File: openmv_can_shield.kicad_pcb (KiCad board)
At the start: 2 copper layers, 75 x 49 mm, 32 parts, among them J1 WAGO_250-204, J2 Pulse_JXD6-0001NL, J3 Conn_01x03, J4 Conn_01x02, J5 Conn_02x03_Odd_Even, J6 Conn_02x05_Odd_Even, J7 Conn_01x02, J8 Conn_01x02, Q1 BSS138, Q2 BSS138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

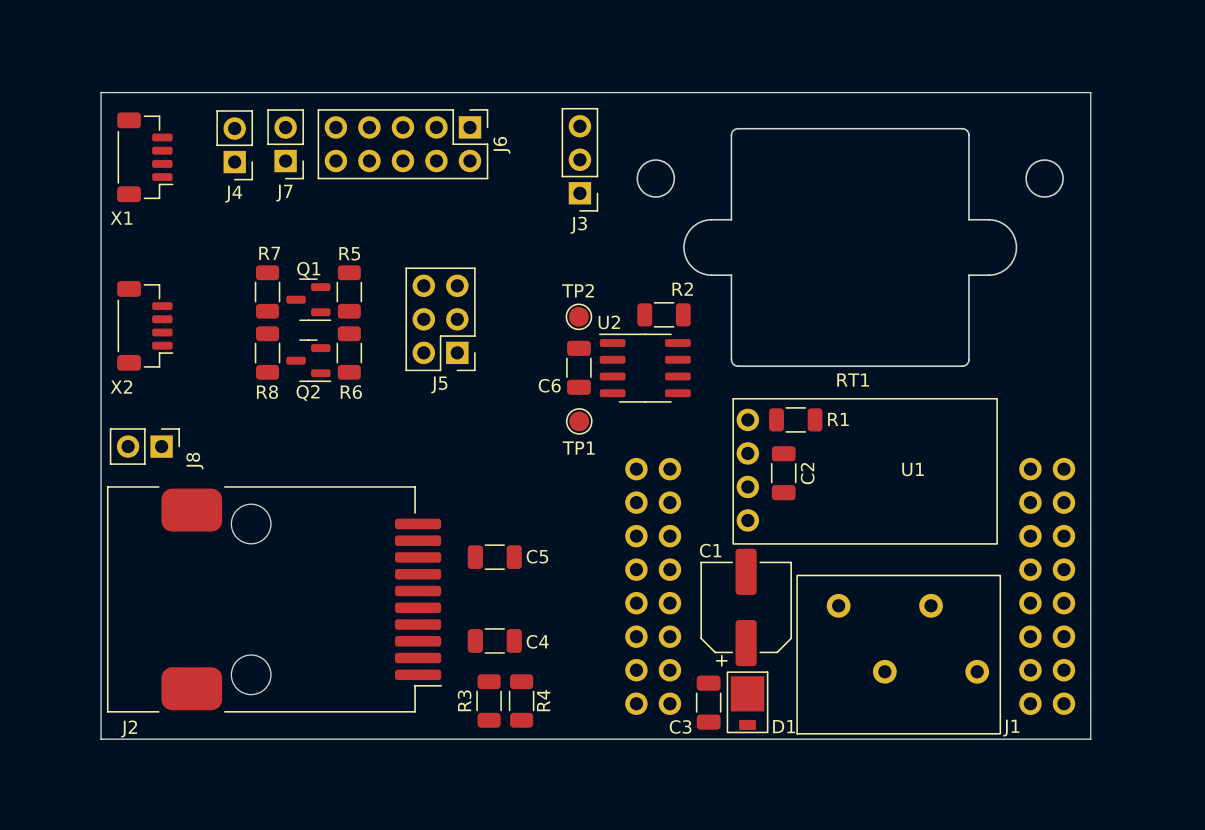
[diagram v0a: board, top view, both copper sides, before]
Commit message: Updated schematics and layout to have complete, DRC clean layout, Gerbers not updated
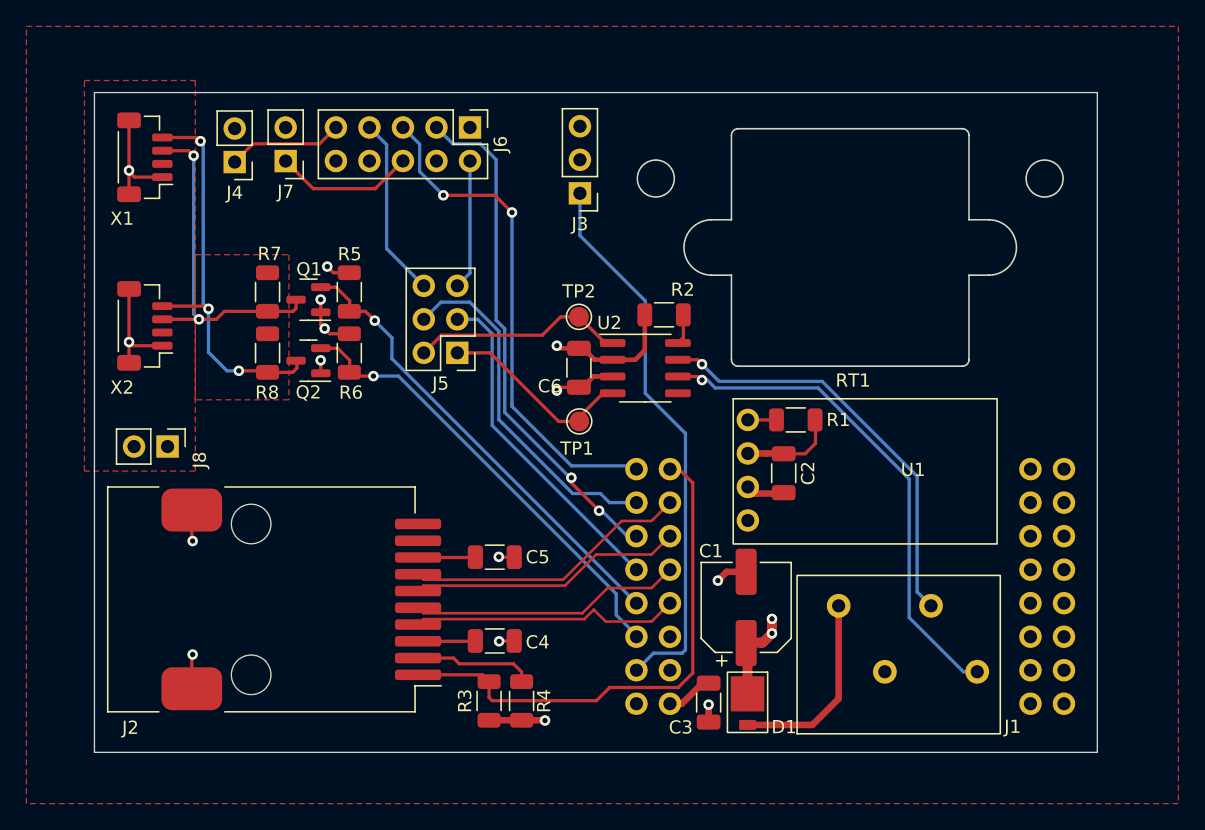
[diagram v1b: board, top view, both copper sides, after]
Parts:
- moved J8 0.45 mm to (84.5, 72.4)
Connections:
- net /ETH_RXN renamed /ETH_RX_N
- net /ETH_RXP renamed /ETH_RX_P
- net /ETH_TXN renamed /ETH_TX_N
- net /ETH_TXP renamed /ETH_TX_P
- J2 pad SH: unconnected-(J2-PadSH) -> GND
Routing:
- net GND: track 0.00 -> 42.9 mm, vias 0 -> 8
- net /AIN: track 0.00 -> 42.3 mm
- net /ETH_LED: track 0.00 -> 39.8 mm
- net /SPI_SCLK: track 0.00 -> 39.1 mm, vias 0 -> 2
- net /SPI_MOSI: track 0.00 -> 38.2 mm, vias 0 -> 2
- net /CAN_L: track 0.00 -> 38.1 mm, vias 0 -> 1
- net /SCL: track 0.00 -> 35.3 mm, vias 0 -> 1
- net /SDA: track 0.00 -> 34.6 mm, vias 0 -> 1
- net /CAN_H: track 0.00 -> 32.0 mm, vias 0 -> 1
- net /SDA_EXT: track 0.00 -> 30.9 mm, vias 0 -> 3
- net /SPI_MISO_CAN_TX: track 0.00 -> 26.9 mm
- net /SCL_EXT: track 0.00 -> 26.2 mm, vias 0 -> 2
- net /SPI_SS_CAN_RX: track 0.00 -> 25.5 mm
- net /ETH_RX_N: track 0.00 -> 21.7 mm
- net /ETH_RX_P: track 0.00 -> 20.8 mm
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- added copper zone on In1.Cu, net +12V
- added copper zone on In1.Cu, net +3.3V
- added copper zone on F.Cu, net +5V
- added copper zone on F.Cu, net /I2C_EXT_VDD
- added copper zone on In2.Cu, net GND
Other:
- board size 75 x 49 mm -> 76 x 50 mm
- copper layers 2 -> 4
